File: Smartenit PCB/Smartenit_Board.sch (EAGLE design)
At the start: 88 parts, among them J1 2X5CONNECTOR1.27MM, Q1 QUARTZ_3.58M_2PIN, U1 SN74LVC1G3157, U2 ADE7953, U3 ESP-WROOM-32

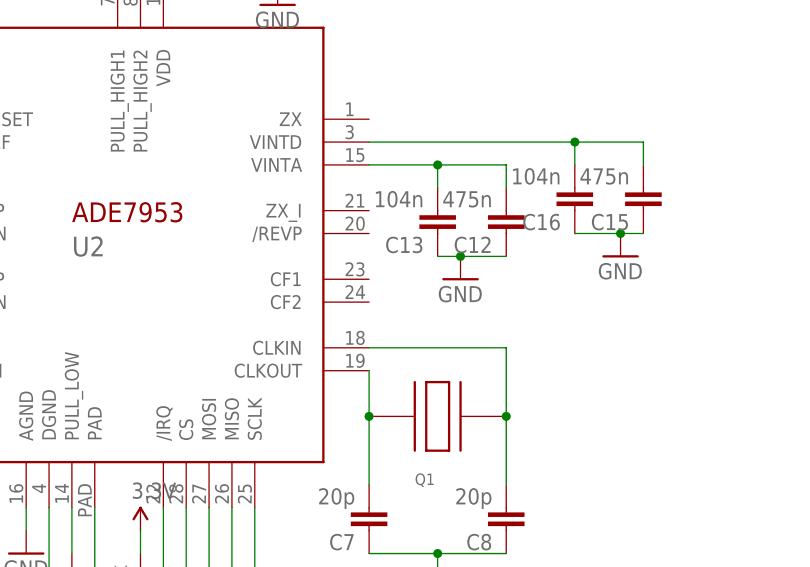
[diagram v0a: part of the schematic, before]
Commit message: Added CF1 and CF2 test points
Last edit for board design for smartenit
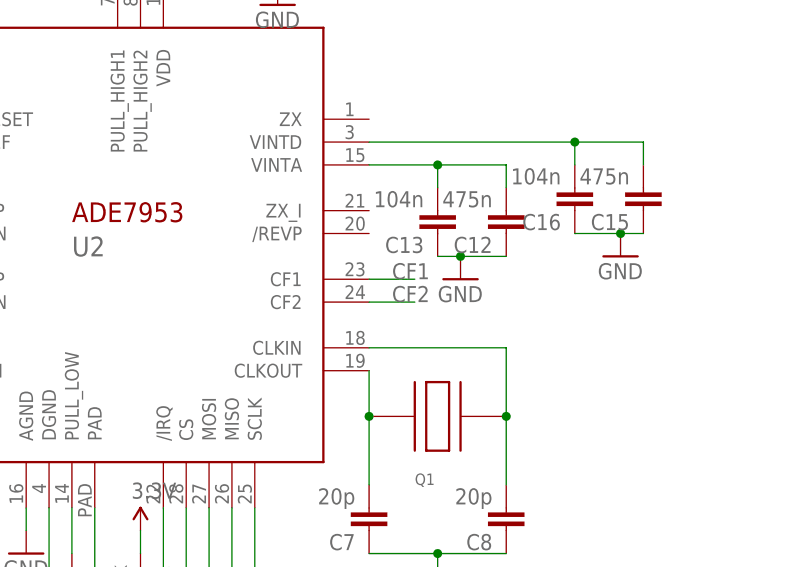
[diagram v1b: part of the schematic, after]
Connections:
- new net CF1: U2.CF1
- new net CF2: U2.CF2
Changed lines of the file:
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@@
+</segment>
+</net>
+<net name="CF1" class="0">
+<segment>
+<pinref part="U2" gate="G$1" pin="CF1"/>
+<wire x1="-175.26" y1="-38.1" x2="-170.18" y2="-38.1" width="0.1524" layer="91"/>
+<label x="-172.72" y="-38.1" size="1.778" layer="95"/>
+</segment>
+</net>
+<net name="CF2" class="0">
+<segment>
+<pinref part="U2" gate="G$1" pin="CF2"/>
+<wire x1="-175.26" y1="-40.64" x2="-170.18" y2="-40.64" width="0.1524" layer="91"/>
+<label x="-172.72" y="-40.64" size="1.778" layer="95"/>
 </segment>
 </net>

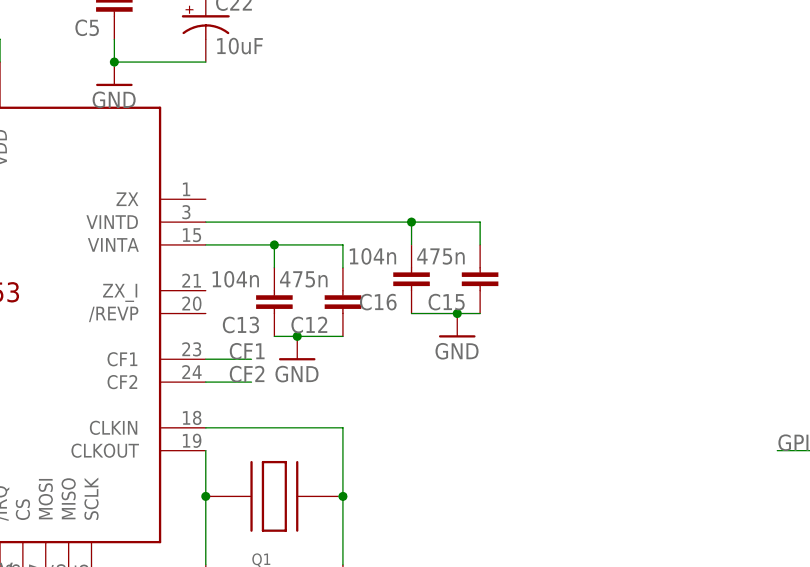
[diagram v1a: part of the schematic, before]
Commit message: Last edits
Added grounds for new resistors and added test points for REVP, ZX, and ZX_I
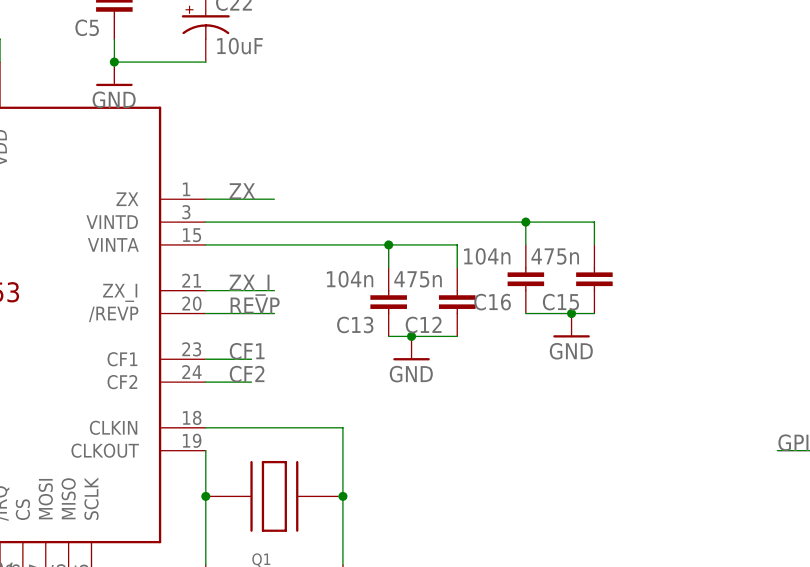
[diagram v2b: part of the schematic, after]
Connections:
- removed net GND: R43.2, R44.1
- new net REVP: U2./REVP
- new net ZX: U2.ZX
- new net ZX_I: U2.ZX_I
- net DGND: now also R43.2, R44.1
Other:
- moved on the sheet: C12, C13, C15, C16
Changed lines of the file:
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@@
 <part name="R43" library="SparkFun-Resistors" deviceset="1KOHM" device="-0603-1/10W-1%" value="4.7k"/>
 <part name="R44" library="SparkFun-Resistors" deviceset="1KOHM" device="-0603-1/10W-1%" value="4.7k"/>
-<part name="DFGND" library="SparkFun" deviceset="GND" device=""/>
-<part name="DGND" library="SparkFun" deviceset="GND" device=""/>
+<part name="GNDI23" library="SparkFun" deviceset="GND" device=""/>
+<part name="GNDI31" library="SparkFun" deviceset="GND" device=""/>
 </parts>
 <sheets>
@@
 <instance part="C17" gate="G$1" x="-292.1" y="-7.62" rot="R180"/>
 <instance part="C18" gate="G$1" x="-292.1" y="-17.78" rot="R180"/>
-<instance part="C13" gate="G$1" x="-165.1" y="-30.48" rot="R180"/>
-<instance part="C12" gate="G$1" x="-157.48" y="-30.48" rot="R180"/>
-<instance part="C16" gate="G$1" x="-149.86" y="-27.94" rot="R180"/>
-<instance part="C15" gate="G$1" x="-142.24" y="-27.94" rot="R180"/>
+<instance part="C13" gate="G$1" x="-152.4" y="-30.48" rot="R180"/>
+<instance part="C12" gate="G$1" x="-144.78" y="-30.48" rot="R180"/>
+<instance part="C16" gate="G$1" x="-137.16" y="-27.94" rot="R180"/>
+<instance part="C15" gate="G$1" x="-129.54" y="-27.94" rot="R180"/>
 <instance part="R31" gate="G$1" x="-261.62" y="-53.34" rot="R270"/>
 <instance part="R23" gate="G$1" x="-233.68" y="-53.34" rot="R270"/>
@@
 <instance part="GNDI14" gate="1" x="-261.62" y="-66.04"/>
 <instance part="GNDI15" gate="1" x="-228.6" y="-66.04"/>
-<instance part="GNDI17" gate="1" x="-147.32" y="-35.56"/>
-<instance part="GNDI18" gate="1" x="-165.1" y="-38.1"/>
+<instance part="GNDI17" gate="1" x="-134.62" y="-35.56"/>
+<instance part="GNDI18" gate="1" x="-152.4" y="-38.1"/>
 <instance part="GNDI19" gate="1" x="-213.36" y="-68.58"/>
 <instance part="GNDI20" gate="1" x="-210.82" y="-86.36"/>
@@
 <instance part="R43" gate="G$1" x="-292.1" y="-73.66" rot="R90"/>
 <instance part="R44" gate="G$1" x="-292.1" y="-96.52" rot="R90"/>
-<instance part="DFGND" gate="1" x="-292.1" y="-63.5" rot="R180"/>
-<instance part="DGND" gate="1" x="-292.1" y="-106.68"/>
+<instance part="GNDI23" gate="1" x="-292.1" y="-106.68"/>
+<instance part="GNDI31" gate="1" x="-292.1" y="-63.5" rot="R180"/>
 </instances>
 <busses>
@@
 <segment>
 <pinref part="U2" gate="G$1" pin="VINTA"/>
-<wire x1="-175.26" y1="-25.4" x2="-167.64" y2="-25.4" width="0.1524" layer="91"/>
+<wire x1="-175.26" y1="-25.4" x2="-154.94" y2="-25.4" width="0.1524" layer="91"/>
 <pinref part="C12" gate="G$1" pin="2"/>
-<wire x1="-160.02" y1="-25.4" x2="-160.02" y2="-27.94" width="0.1524" layer="91"/>
+<wire x1="-147.32" y1="-25.4" x2="-147.32" y2="-27.94" width="0.1524" layer="91"/>
 <pinref part="C13" gate="G$1" pin="2"/>
-<wire x1="-167.64" y1="-27.94" x2="-167.64" y2="-25.4" width="0.1524" layer="91"/>
-<wire x1="-167.64" y1="-25.4" x2="-160.02" y2="-25.4" width="0.1524" layer="91"/>
-<junction x="-167.64" y="-25.4"/>
+<wire x1="-154.94" y1="-27.94" x2="-154.94" y2="-25.4" width="0.1524" layer="91"/>
+<wire x1="-154.94" y1="-25.4" x2="-147.32" y2="-25.4" width="0.1524" layer="91"/>
+<junction x="-154.94" y="-25.4"/>
 </segment>
 </net>
@@
 <pinref part="C15" gate="G$1" pin="2"/>
 <pinref part="U2" gate="G$1" pin="VINTD"/>
-<wire x1="-144.78" y1="-25.4" x2="-144.78" y2="-22.86" width="0.1524" layer="91"/>
-<wire x1="-144.78" y1="-22.86" x2="-152.4" y2="-22.86" width="0.1524" layer="91"/>
+<wire x1="-132.08" y1="-25.4" x2="-132.08" y2="-22.86" width="0.1524" layer="91"/>
+<wire x1="-132.08" y1="-22.86" x2="-139.7" y2="-22.86" width="0.1524" layer="91"/>
 <pinref part="C16" gate="G$1" pin="2"/>
-<wire x1="-152.4" y1="-22.86" x2="-175.26" y2="-22.86" width="0.1524" layer="91"/>
-<wire x1="-152.4" y1="-25.4" x2="-152.4" y2="-22.86" width="0.1524" layer="91"/>
-<junction x="-152.4" y="-22.86"/>
+<wire x1="-139.7" y1="-22.86" x2="-175.26" y2="-22.86" width="0.1524" layer="91"/>
+<wire x1="-139.7" y1="-25.4" x2="-139.7" y2="-22.86" width="0.1524" layer="91"/>
+<junction x="-139.7" y="-22.86"/>
 </segment>
 </net>
@@
 <segment>
 <pinref part="C16" gate="G$1" pin="1"/>
-<wire x1="-152.4" y1="-33.02" x2="-147.32" y2="-33.02" width="0.1524" layer="91"/>
+<wire x1="-139.7" y1="-33.02" x2="-134.62" y2="-33.02" width="0.1524" layer="91"/>
 <pinref part="C15" gate="G$1" pin="1"/>
-<wire x1="-147.32" y1="-33.02" x2="-144.78" y2="-33.02" width="0.1524" layer="91"/>
-<junction x="-147.32" y="-33.02"/>
+<wire x1="-134.62" y1="-33.02" x2="-132.08" y2="-33.02" width="0.1524" layer="91"/>
+<junction x="-134.62" y="-33.02"/>
 <pinref part="GNDI17" gate="1" pin="GND"/>
 </segment>
@@
 <wire x1="-205.74" y1="-91.44" x2="-205.74" y2="-63.5" width="0.1524" layer="91"/>
 </segment>
+<segment>
+<pinref part="R43" gate="G$1" pin="2"/>
+<wire x1="-292.1" y1="-68.58" x2="-292.1" y2="-66.04" width="0.1524" layer="91"/>
+<pinref part="GNDI31" gate="1" pin="GND"/>
+</segment>
+<segment>
+<pinref part="R44" gate="G$1" pin="1"/>
+<wire x1="-292.1" y1="-101.6" x2="-292.1" y2="-104.14" width="0.1524" layer="91"/>
+<pinref part="GNDI23" gate="1" pin="GND"/>
+</segment>
 </net>
 <net name="AGND" class="0">
 <segment>
 <pinref part="C13" gate="G$1" pin="1"/>
-<wire x1="-167.64" y1="-35.56" x2="-165.1" y2="-35.56" width="0.1524" layer="91"/>
+<wire x1="-154.94" y1="-35.56" x2="-152.4" y2="-35.56" width="0.1524" layer="91"/>
 <pinref part="C12" gate="G$1" pin="1"/>
-<wire x1="-165.1" y1="-35.56" x2="-160.02" y2="-35.56" width="0.1524" layer="91"/>
-<junction x="-165.1" y="-35.56"/>
+<wire x1="-152.4" y1="-35.56" x2="-147.32" y2="-35.56" width="0.1524" layer="91"/>
+<junction x="-152.4" y="-35.56"/>
 <pinref part="GNDI18" gate="1" pin="GND"/>
 </segment>
@@
 </segment>
 </net>
-<net name="GND" class="0">
-<segment>
-<pinref part="R43" gate="G$1" pin="2"/>
-<pinref part="DFGND" gate="1" pin="GND"/>
-<wire x1="-292.1" y1="-68.58" x2="-292.1" y2="-66.04" width="0.1524" layer="91"/>
-</segment>
-<segment>
-<pinref part="R44" gate="G$1" pin="1"/>
-<pinref part="DGND" gate="1" pin="GND"/>
-<wire x1="-292.1" y1="-101.6" x2="-292.1" y2="-104.14" width="0.1524" layer="91"/>
-</segment>
-</net>
 <net name="CF1" class="0">
 <segment>
@@
 </segment>
 </net>
+<net name="ZX" class="0">
+<segment>
+<pinref part="U2" gate="G$1" pin="ZX"/>
+<wire x1="-175.26" y1="-20.32" x2="-167.64" y2="-20.32" width="0.1524" layer="91"/>
+<label x="-172.72" y="-20.32" size="1.778" layer="95"/>
+</segment>
+</net>
+<net name="ZX_I" class="0">
+<segment>
+<pinref part="U2" gate="G$1" pin="ZX_I"/>
+<wire x1="-175.26" y1="-30.48" x2="-167.64" y2="-30.48" width="0.1524" layer="91"/>
+<label x="-172.72" y="-30.48" size="1.778" layer="95"/>
+</segment>
+</net>
+<net name="REVP" class="0">
+<segment>
+<pinref part="U2" gate="G$1" pin="/REVP"/>
+<wire x1="-175.26" y1="-33.02" x2="-167.64" y2="-33.02" width="0.1524" layer="91"/>
+<label x="-172.72" y="-33.02" size="1.778" layer="95"/>
+</segment>
+</net>

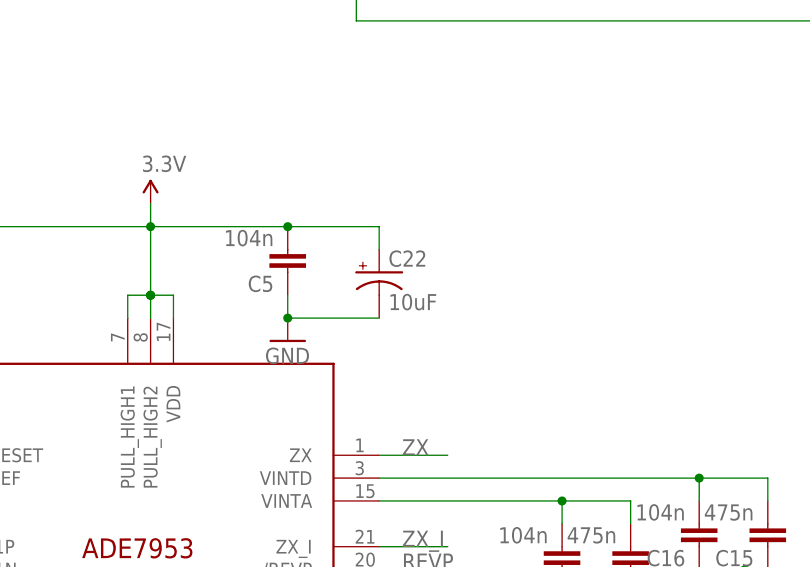
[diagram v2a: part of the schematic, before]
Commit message: updated cap sizes
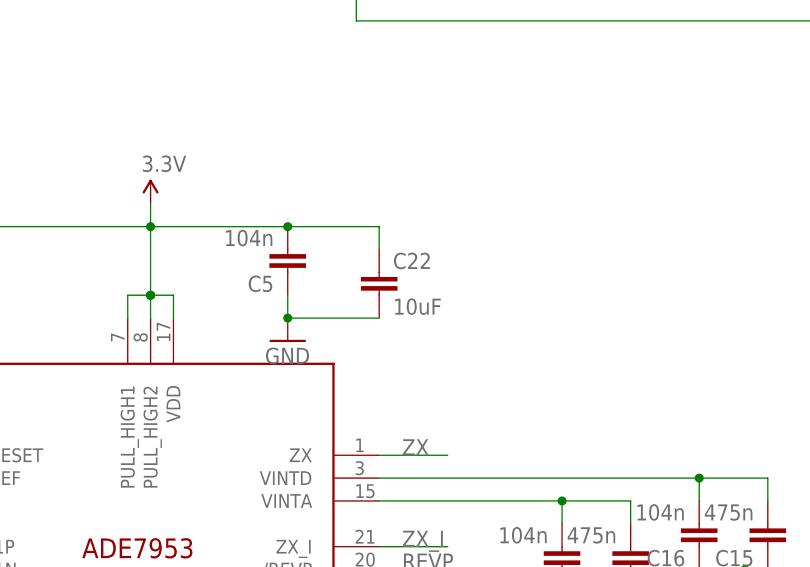
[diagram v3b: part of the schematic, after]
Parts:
- C2: device SparkFun:CAP0603-CAP -> SparkFun:CAP0805
- C22: device SparkFun:CAP_POL1206 -> SparkFun-Capacitors:10UF-0805-10V-10%
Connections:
- net 3.3V: now also C22.1; no longer C22.+
- net DGND: now also C22.2; no longer C22.-

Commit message: added JP2 header
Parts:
- added JP2: 2MM_CONN6, Smart_Charger:2MM_CONN6
- added R45, R46: 4.7k, Nizanlib:0402-RES
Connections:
- new net GND: JP2.PIN4
- new net SCL: JP2.PIN2, R45.1, U3.IO17
- new net SDA: JP2.PIN1, R46.1, U3.IO5
- net 3.3V: now also JP2.PIN3, R45.2, R46.2
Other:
- note added: "I2C AUX"
- note added: "Label pins on silkscreen"
- note added: "Mark Pin 1 on the layout for JP2"

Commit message: added notes
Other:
- note added: "Change to 4-pin header"
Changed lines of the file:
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@@
 <text x="-248.92" y="22.86" size="1.778" layer="91">Mark Pin 1 on the layout for JP2</text>
 <text x="-220.98" y="40.64" size="1.778" layer="91">Label pins on silkscreen</text>
+<text x="-223.52" y="27.94" size="1.778" layer="91">Change to 4-pin header</text>
 </plain>
 <instances>

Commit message: fixed labeling and other stuff
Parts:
- renumbered Q1 to XTAL
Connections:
- net BLUE_LED: no longer U3.IO22
- net DGND: no longer D3.P
- net GND: now also D3.P
- net SDA: now also U3.IO22
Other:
- note added: "* Mode control bootstrap operational pins [EN, GPIOs 0, 2, 12, 15]"
- note added: "1.1"
- note added: "3.58 MHz"
- note added: "Add index mark for pin 1 in layout"
- note added: "Check this 4-junction connections"
- note added: "Common anode bicolor LED"
- note added: "Created by: Andy Begey, Brandon Metcalf"
- note added: "EN RLY DVR"
- note added: "ESP32 EVSE Smart Charger Controller"
- note added: "May 3, 20218"
- note added: "Q2"
- note added: "Refer to datasheet for AGND/DGND connection on PCB"
- note added: "TX/RX crossover prior to header"
- note removed: "IO0, IO2, IO5 are bootstrapping pins. DO NOT USE THEM!"
- moved on the sheet: C10, C11, C19, C2, C21, C22, C3, C5, C9, R22, R31, R39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
